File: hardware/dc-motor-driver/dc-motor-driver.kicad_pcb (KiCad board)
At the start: 2 copper layers, 94 x 100 mm, 85 parts, among them J10 OQ0232510000G, J11 OQ0232510000G, J12 OQ0232510000G, J13 OQ0232510000G, J14 54-00274, J2 VIN, J3 DE9, J4 MOT, J5 MOT, J6 MOT, J7 MOT, J8 MOT, J9 MOT, U1 DRV8874PWPR, U2 DRV8874PWPR, U3 DRV8874PWPR, U4 DRV8874PWPR, U5 DRV8874PWPR, U6 DRV8874PWPR, U7 SP3485CN, U8 SP3485CN

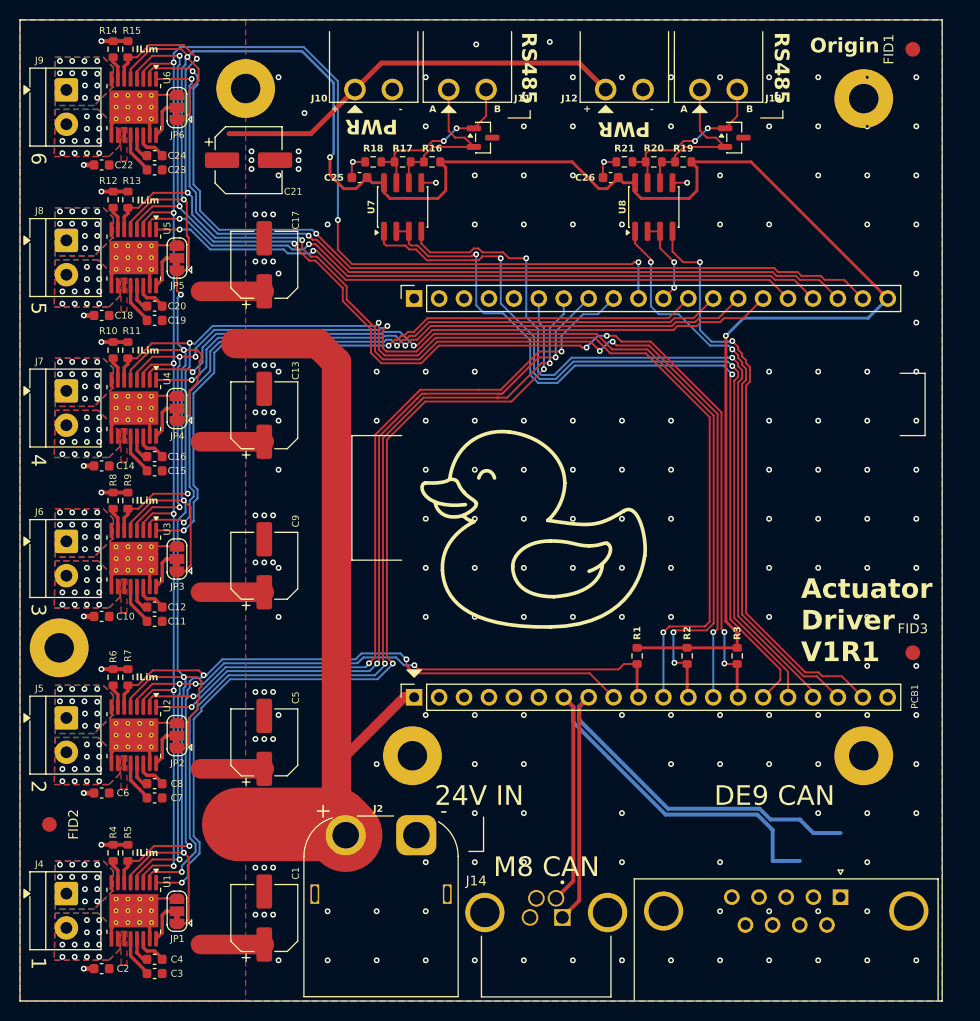
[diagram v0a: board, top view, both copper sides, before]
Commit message: silkscreen additions
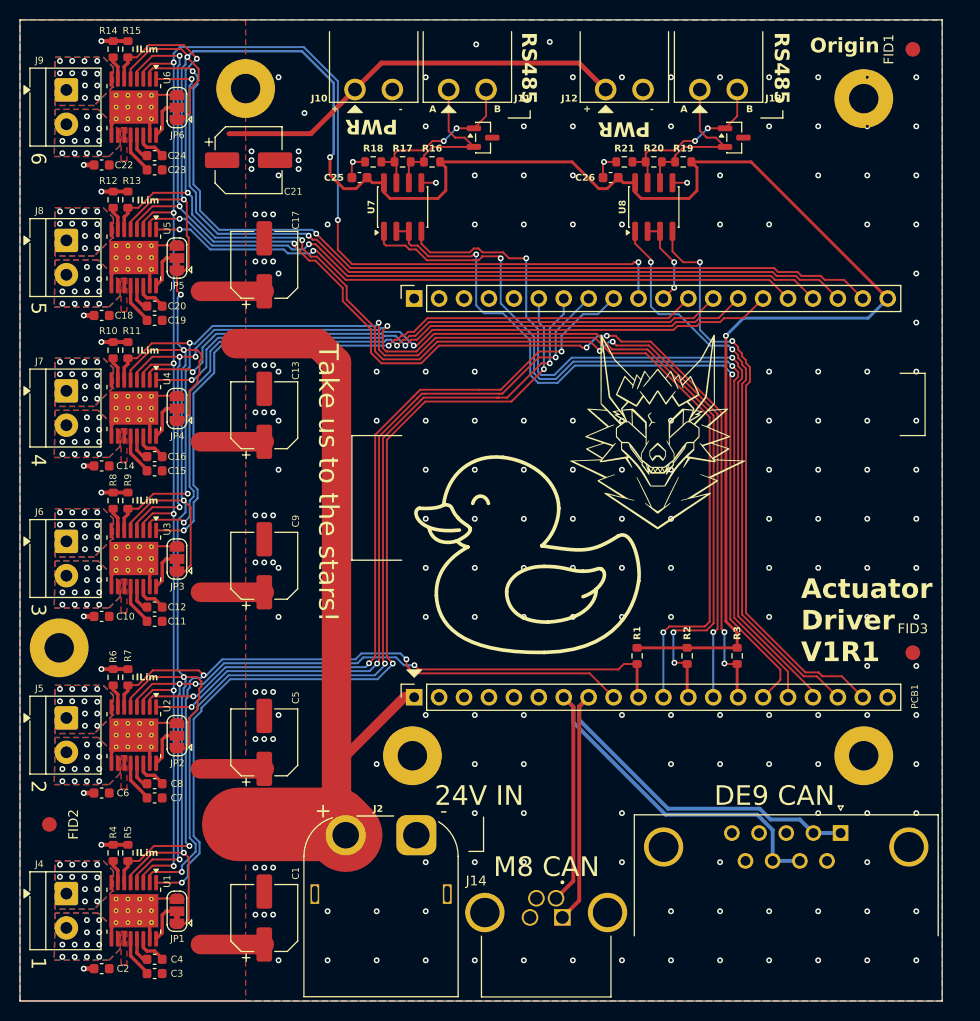
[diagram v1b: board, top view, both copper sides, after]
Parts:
- added G***: LOGO, LOGO, F.Cu at (165.0, 83.1)
- moved J3 6.53 mm to (183.6, 122.9)
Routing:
- net GND: vias 211 -> 212
- net /CAN_H: vias 1 -> 0
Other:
- board text added: "Take us to the stars!"

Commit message: fixed footprint library and changed connectors
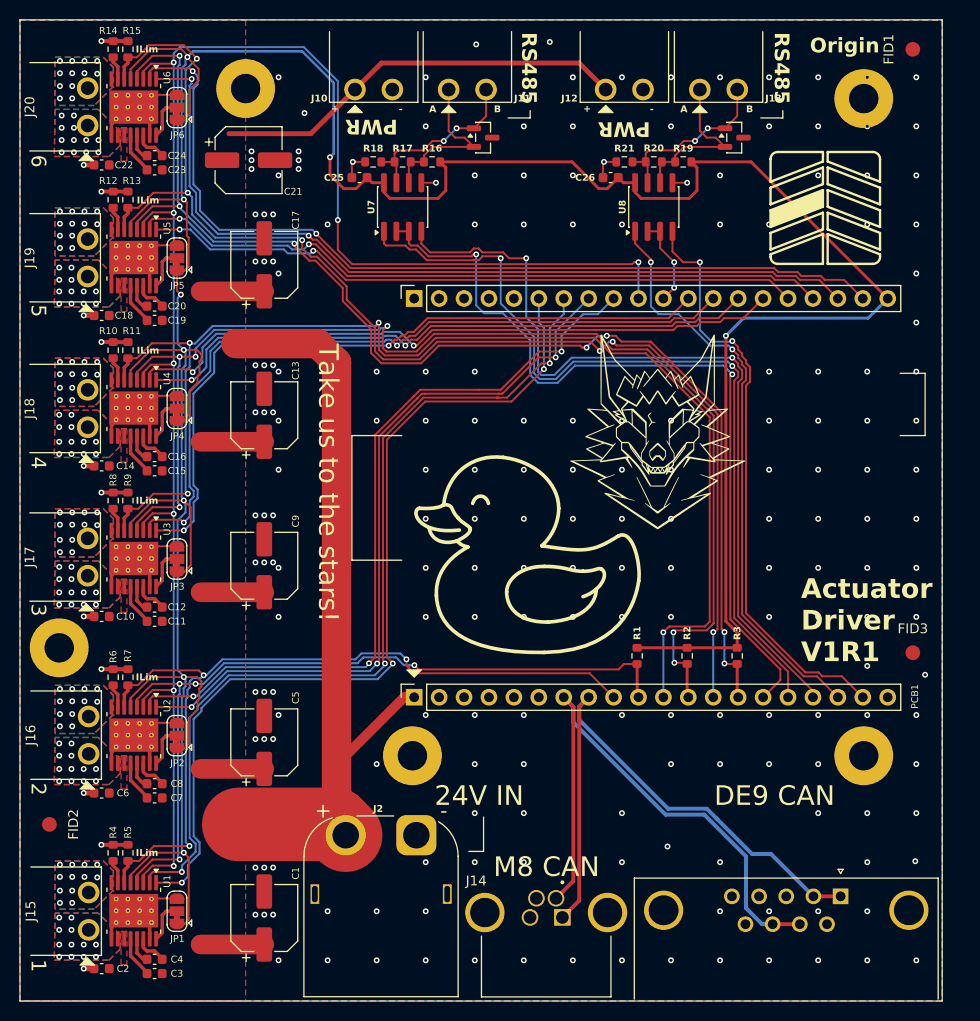
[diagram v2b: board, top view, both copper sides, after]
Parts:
- removed J4, J5, J6, J7, J8, J9: MOT, TerminalBlock_4Ucon:TerminalBlock_4Ucon_1x02_P3.50mm_Horizontal
- added J15: OQ0232510000G, ConnectorsOther:AnyTek_OQ_3.81mm_90_2P_TriangleKeyLock, F.Cu at (103.6, 130.8)
- added J16: OQ0232510000G, ConnectorsOther:AnyTek_OQ_3.81mm_90_2P_TriangleKeyLock, F.Cu at (103.6, 112.9)
- added J17: OQ0232510000G, ConnectorsOther:AnyTek_OQ_3.81mm_90_2P_TriangleKeyLock, F.Cu at (103.5, 94.8)
- added J18: OQ0232510000G, ConnectorsOther:AnyTek_OQ_3.81mm_90_2P_TriangleKeyLock, F.Cu at (103.5, 79.6)
- added J19: OQ0232510000G, ConnectorsOther:AnyTek_OQ_3.81mm_90_2P_TriangleKeyLock, F.Cu at (103.5, 64.2)
- added J20: OQ0232510000G, ConnectorsOther:AnyTek_OQ_3.81mm_90_2P_TriangleKeyLock, F.Cu at (103.5, 48.9)
- moved J3 6.45 mm to (183.6, 129.3)
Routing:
- net /CAN_H: track 55.4 -> 59.3 mm
- net /CAN_L: track 57.7 -> 60.6 mm

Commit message: manufacture ready
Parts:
- removed J14: 54-00274, ConnectorsOther:Tensility_M8_Socket_4P_Shielded_A
- added J1: ~, ConnectorsOther:Tensility_M8_Socket_4P_Shielded_A, F.Cu at (153.6, 131.2)
- moved C1 0.20 mm to (124.7, 131.5)
- moved J2 0.10 mm to (140.3, 123.1)
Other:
- board text added: "ANTENNA"
- board text added: "USB"
